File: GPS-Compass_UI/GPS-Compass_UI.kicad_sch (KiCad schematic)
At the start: 12 parts, among them SW1 EXT, SW2 EXT, SW4 EXT

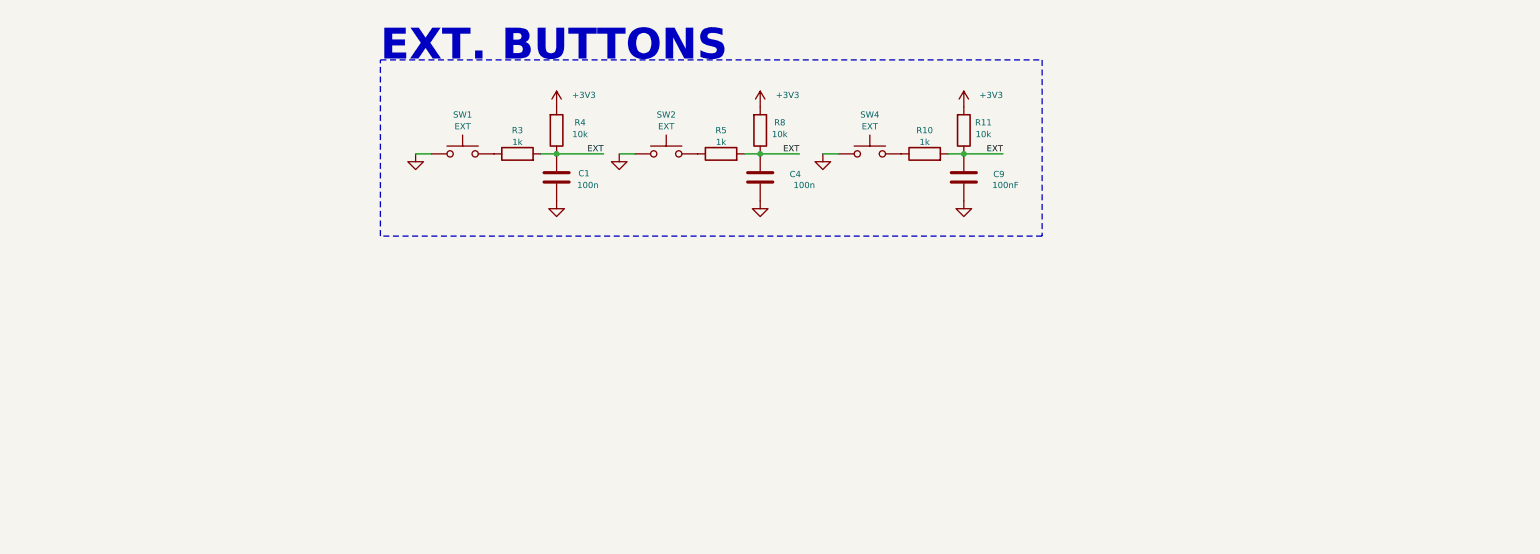
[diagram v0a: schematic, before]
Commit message: UI layout and routing
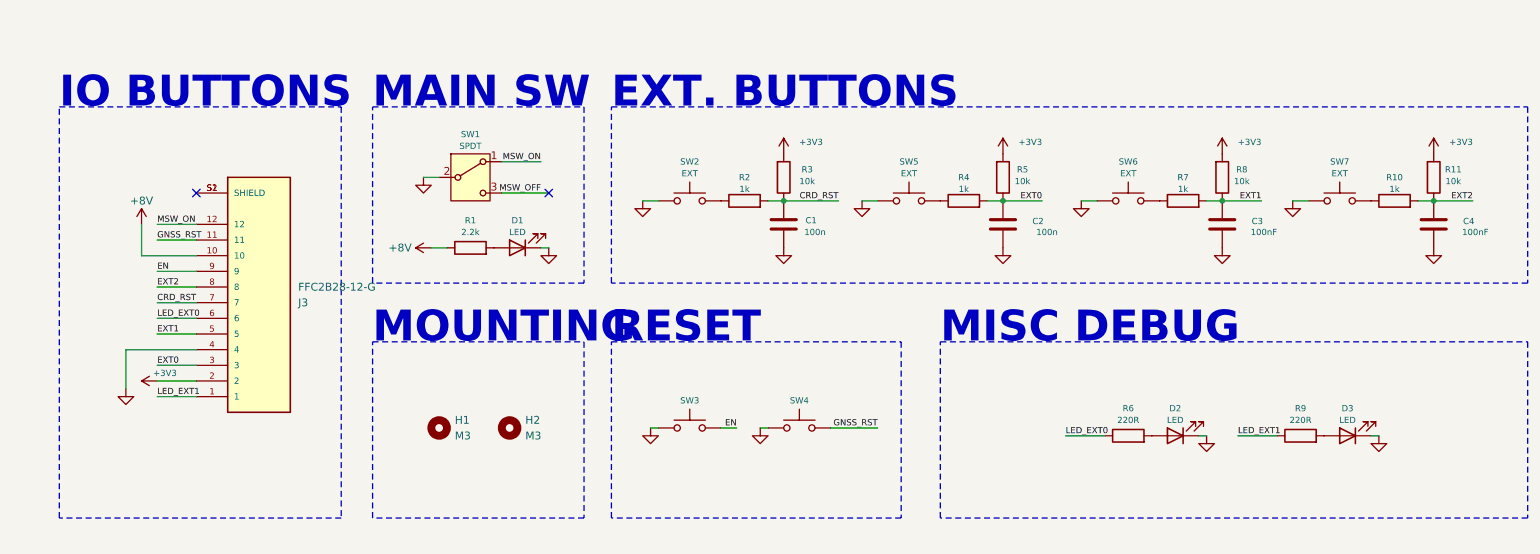
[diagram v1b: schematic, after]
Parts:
- added C4: 100nF, Capacitor_SMD:C_0805_2012Metric, symbol Device:C
- added D1, D2, D3: LED, Connector_Wire:SolderWire-0.1sqmm_1x02_P3.6mm_D0.4mm_OD1mm_Relief, symbol Device:LED
- added H1, H2: M3, MountingHole:MountingHole_3.2mm_M3, symbol Mechanical:MountingHole
- added J3: FFC2B28-12-G, gps-compass_brd:GCT_FFC2B28-12-G, symbol gps-compass_sch:FFC2B28-12-G
- added R1: 2.2k, Resistor_SMD:R_0805_2012Metric, symbol Device:R
- added R10: 1k, Resistor_SMD:R_0805_2012Metric, symbol Device:R
- added R11: 10k, Resistor_SMD:R_0805_2012Metric, symbol Device:R
- added R6, R9: 220R, Resistor_SMD:R_0805_2012Metric, symbol Device:R
- added SW1: SPDT, Connector_Wire:SolderWire-0.1sqmm_1x02_P3.6mm_D0.4mm_OD1mm_Relief, symbol Switch:SW_SPDT
- added SW3, SW4: RESET, Connector_Wire:SolderWire-0.1sqmm_1x02_P3.6mm_D0.4mm_OD1mm_Relief, symbol Switch:SW_Push
- added SW7: EXT, Connector_Wire:SolderWire-0.1sqmm_1x02_P3.6mm_D0.4mm_OD1mm_Relief, symbol Switch:SW_Push
- renumbered C4 to C2, C9 to C3, R3 to R2, R4 to R3, R5 to R4, R8 to R5, R10 to R7, R11 to R8, SW1 to SW2, SW2 to SW5, SW4 to SW6
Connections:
- net +3V3: now also J3.2, R11.2
- net GND: now also C4.1, D1.1 (K), D2.1 (K), D3.1 (K), J3.4, SW1.2 (B), SW3.1, SW4.1, SW7.1
- removed net EXT: C1.2, C2.2, C3.2, R2.2, R3.1, R4.2, R5.1, R7.2, R8.1
- new net: D1.2 (A), R1.2
- new net: D3.2 (A), R9.2
- new net: R10.1, SW7.2
- new net: J3.S1 (SHIELD), J3.S2 (SHIELD)
- new net: D2.2 (A), R6.2
- new net +8V: J3.10, R1.1
- new net CRD_RST: C1.2, J3.7, R2.2, R3.1
- new net EN: J3.9, SW3.2
- new net EXT0: C2.2, J3.3, R4.2, R5.1
- new net EXT1: C3.2, J3.5, R7.2, R8.1
- new net EXT2: C4.2, J3.8, R10.2, R11.1
- new net GNSS_RST: J3.11, SW4.2
- new net LED_EXT0: J3.6, R6.1
- new net LED_EXT1: J3.1, R9.1
- new net MSW_OFF: SW1.3 (C)
- new net MSW_ON: J3.12, SW1.1 (A)
- no-connect marks 0 -> 2
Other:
- note added: "IO BUTTONS"
- note added: "MAIN SW"
- note added: "MISC DEBUG"
- note added: "MOUNTING"
- note added: "RESET"
- moved on the sheet: C1, C2, C3, R2, R3, R4, R5, R7, R8, SW2, SW5, SW6

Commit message: GPS Compass - schematic
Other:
- note added: "FFC"
- note removed: "IO BUTTONS"
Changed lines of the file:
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@@
 		)
 	)
-	(text "IO BUTTONS"
+	(text "FFC"
 		(exclude_from_sim no)
 		(at 31.115 52.705 0)
@@
 		(dnp no)
 		(property "Reference" "J3"
-			(at 69.85 83.8201 0)
+			(at 54.61 106.045 0)
 			(effects
 				(font
@@
 		)
 		(property "Value" "FFC2B28-12-G"
-			(at 69.85 81.2801 0)
-			(effects
-				(font
+			(at 54.61 103.505 0)
+			(effects
+				(font

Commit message: UI changes
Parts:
- removed D3: LED, Connector_Wire:SolderWire-0.1sqmm_1x02_P3.6mm_D0.4mm_OD1mm_Relief, symbol Device:LED
- removed R9: 220R, Resistor_SMD:R_0805_2012Metric, symbol Device:R
- added D1: LED, Connector_Wire:SolderWire-0.1sqmm_1x02_P3.6mm_D0.4mm_OD1mm_Relief, symbol Device:LED
- added R2: 2.2k, Resistor_SMD:R_0805_2012Metric, symbol Device:R
- added SW2: SW_SPDT, Connector_Wire:SolderWire-0.1sqmm_1x02_P3.6mm_D0.4mm_OD1mm_Relief, symbol Switch:SW_SPDT
- renumbered D1 to D2, D2 to D3, J3 to J1, R2 to R3, R3 to R4, R4 to R5, R5 to R6, R6 to R7, R7 to R8, R8 to R9, SW2 to SW3, SW3 to SW4, SW4 to SW5, SW5 to SW6, SW6 to SW7, SW7 to SW8
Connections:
- net +3V3: now also R1.1, SW2.2 (B)
- net GND: now also D1.1 (K); no longer D2.1 (K)
- net GNSS_RST: now also J1.10; no longer J1.11
- net MSW_ON: now also D2.1 (K), J1.11; no longer J1.12
- net DB_1: now reaches R3.1, SW3.2
- net DB_3: now reaches R8.1, SW7.2
- net DB_0: now reaches R10.1, SW8.2
- net DB_2: now reaches R5.1, SW6.2
- removed net +8V: J1.10, R1.1
- net CRD_RST renamed DBNCD_1
- net EXT0 renamed DBNCD_2
- net DBNCD_2: now also J1.5; no longer J1.3
- net EXT1 renamed DBNCD_3
- net DBNCD_3: now also J1.3; no longer J1.5
- net EXT2 renamed DBNCD_0
- net LED_EXT0 renamed LED_EXT
- net LED_EXT1 renamed OTG_ON
- net OTG_ON: now also R2.1, SW2.1 (A)
- new net: D1.2 (A), R2.2
- new net OTG_OFF: SW2.3 (C)
- no-connect marks 2 -> 3
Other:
- note added: "LED"
- note removed: "MISC DEBUG"
- moved on the sheet: C1, C2, C3, C4, D2, D3, H1, H2, J1, R1, R10, R11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

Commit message: jkolsd
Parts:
- renumbered C4 to C1, C1 to C2, C2 to C3, C3 to C4, R8 to R10, R9 to R11, R10 to R3, R11 to R4, R3 to R5, R4 to R6, R5 to R8, R6 to R9, SW4 to SW3, SW8 to SW4, SW3 to SW6, SW6 to SW7, SW7 to SW8
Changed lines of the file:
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@@
 		(on_board yes)
 		(dnp no)
-		(property "Reference" "#PWR020"
+		(property "Reference" "#PWR010"
 			(at 143.51 62.23 0)
 			(effects
@@
 			(project "GPS-Compass_UI"
 				(path "/2171b68c-3635-466a-9c8f-785127caa9a5"
-					(reference "#PWR020")
+					(reference "#PWR010")
 					(unit 1)
 				)
@@
 		(on_board yes)
 		(dnp no)
-		(property "Reference" "SW4"
+		(property "Reference" "SW3"
 			(at 125.73 99.695 0)
 			(effects
@@
 			(project "GPS-Compass_UI"
 				(path "/2171b68c-3635-466a-9c8f-785127caa9a5"
-					(reference "SW4")
+					(reference "SW3")
 					(unit 1)
 				)
@@
 		(on_board yes)
 		(dnp no)
-		(property "Reference" "SW3"
+		(property "Reference" "SW6"
 			(at 162.56 59.69 0)
 			(effects
@@
 			(project "GPS-Compass_UI"
 				(path "/2171b68c-3635-466a-9c8f-785127caa9a5"
-					(reference "SW3")
+					(reference "SW6")
 					(unit 1)
 				)
@@
 		(on_board yes)
 		(dnp no)
-		(property "Reference" "R11"
+		(property "Reference" "R4"
 			(at 146.685 60.96 0)
 			(effects
@@
 			(project "GPS-Compass_UI"
 				(path "/2171b68c-3635-466a-9c8f-785127caa9a5"
-					(reference "R11")
+					(reference "R4")
 					(unit 1)
 				)
@@
 		(on_board yes)
 		(dnp no)
-		(property "Reference" "SW7"
+		(property "Reference" "SW8"
 			(at 228.6 59.69 0)
 			(effects
@@
 			(project "GPS-Compass_UI"
 				(path "/2171b68c-3635-466a-9c8f-785127caa9a5"
-					(reference "SW7")
+					(reference "SW8")
 					(unit 1)
 				)
@@
 		(on_board yes)
 		(dnp no)
-		(property "Reference" "#PWR010"
+		(property "Reference" "#PWR013"
 			(at 179.07 62.23 0)
 			(effects
@@
 			(project "GPS-Compass_UI"
 				(path "/2171b68c-3635-466a-9c8f-785127caa9a5"
-					(reference "#PWR010")
+					(reference "#PWR013")
 					(unit 1)
 				)
@@
 		(on_board yes)
 		(dnp no)
-		(property "Reference" "C3"
+		(property "Reference" "C4"
 			(at 250.19 69.215 0)
 			(effects
@@
 			(project "GPS-Compass_UI"
 				(path "/2171b68c-3635-466a-9c8f-785127caa9a5"
-					(reference "C3")
+					(reference "C4")
 					(unit 1)
 				)
@@
 		(on_board yes)
 		(dnp no)
-		(property "Reference" "R8"
+		(property "Reference" "R10"
 			(at 238.76 62.23 90)
 			(effects
@@
 			(project "GPS-Compass_UI"
 				(path "/2171b68c-3635-466a-9c8f-785127caa9a5"
-					(reference "R8")
+					(reference "R10")
 					(unit 1)
 				)
@@
 		(on_board yes)
 		(dnp no)
-		(property "Reference" "C2"
+		(property "Reference" "C3"
 			(at 216.535 69.215 0)
 			(effects
@@
 			(project "GPS-Compass_UI"
 				(path "/2171b68c-3635-466a-9c8f-785127caa9a5"
-					(reference "C2")
+					(reference "C3")
 					(unit 1)
 				)
@@
 		(on_board yes)
 		(dnp no)
-		(property "Reference" "C4"
+		(property "Reference" "C1"
 			(at 148.59 69.215 0)
 			(effects
@@
 			(project "GPS-Compass_UI"
 				(path "/2171b68c-3635-466a-9c8f-785127caa9a5"
-					(reference "C4")
+					(reference "C1")
 					(unit 1)
 				)
@@
 		(on_board yes)
 		(dnp no)
-		(property "Reference" "#PWR017"
+		(property "Reference" "#PWR020"
 			(at 245.11 62.23 0)
 			(effects
@@
 			(project "GPS-Compass_UI"
 				(path "/2171b68c-3635-466a-9c8f-785127caa9a5"
-					(reference "#PWR017")
+					(reference "#PWR020")
 					(unit 1)
 				)
@@
 		(on_board yes)
 		(dnp no)
-		(property "Reference" "#PWR011"
+		(property "Reference" "#PWR014"
 			(at 179.07 80.01 0)
 			(effects
@@
 			(project "GPS-Compass_UI"
 				(path "/2171b68c-3635-466a-9c8f-785127caa9a5"
-					(reference "#PWR011")
+					(reference "#PWR014")
 					(unit 1)
 				)
@@
 		(on_board yes)
 		(dnp no)
-		(property "Reference" "SW8"
+		(property "Reference" "SW4"
 			(at 127 59.69 0)
 			(effects
@@
 			(project "GPS-Compass_UI"
 				(path "/2171b68c-3635-466a-9c8f-785127caa9a5"
-					(reference "SW8")
+					(reference "SW4")
 					(unit 1)
 				)
@@
 		(on_board yes)
 		(dnp no)
-		(property "Reference" "R9"
+		(property "Reference" "R11"
 			(at 248.285 60.96 0)
 			(effects
@@
 			(project "GPS-Compass_UI"
 				(path "/2171b68c-3635-466a-9c8f-785127caa9a5"
-					(reference "R9")
+					(reference "R11")
 					(unit 1)
 				)
@@
 		(on_board yes)
 		(dnp no)
-		(property "Reference" "SW6"
+		(property "Reference" "SW7"
 			(at 195.58 59.69 0)
 			(effects
@@
 			(project "GPS-Compass_UI"
 				(path "/2171b68c-3635-466a-9c8f-785127caa9a5"
-					(reference "SW6")
+					(reference "SW7")
 					(unit 1)
 				)
@@
 		(on_board yes)
 		(dnp no)
-		(property "Reference" "#PWR015"
+		(property "Reference" "#PWR019"
 			(at 222.25 72.39 0)
 			(effects
@@
 			(project "GPS-Compass_UI"
 				(path "/2171b68c-3635-466a-9c8f-785127caa9a5"
-					(reference "#PWR015")
+					(reference "#PWR019")
 					(unit 1)
 				)
@@
 		(on_board yes)
 		(dnp no)
-		(property "Reference" "#PWR014"
+		(property "Reference" "#PWR018"
 			(at 212.09 80.01 0)
 			(effects
@@
 			(project "GPS-Compass_UI"
 				(path "/2171b68c-3635-466a-9c8f-785127caa9a5"
-					(reference "#PWR014")
+					(reference "#PWR018")
 					(unit 1)
 				)
@@
 		(on_board yes)
 		(dnp no)
-		(property "Reference" "R6"
+		(property "Reference" "R9"
 			(at 215.265 60.96 0)
 			(effects
@@
 			(project "GPS-Compass_UI"
 				(path "/2171b68c-3635-466a-9c8f-785127caa9a5"
-					(reference "R6")
+					(reference "R9")
 					(unit 1)
 				)
@@
 		(on_board yes)
 		(dnp no)
-		(property "Reference" "C1"
+		(property "Reference" "C2"
 			(at 182.88 69.215 0)
 			(effects
@@
 			(project "GPS-Compass_UI"
 				(path "/2171b68c-3635-466a-9c8f-785127caa9a5"
-					(reference "C1")
+					(reference "C2")
 					(unit 1)
 				)
@@
 		(on_board yes)
 		(dnp no)
-		(property "Reference" "R5"
+		(property "Reference" "R8"
 			(at 205.74 62.23 90)
 			(effects
@@
 			(project "GPS-Compass_UI"
 				(path "/2171b68c-3635-466a-9c8f-785127caa9a5"
-					(reference "R5")
+					(reference "R8")
 					(unit 1)
 				)
@@
 		(on_board yes)
 		(dnp no)
-		(property "Reference" "#PWR013"
+		(property "Reference" "#PWR017"
 			(at 212.09 62.23 0)
 			(effects
@@
 			(project "GPS-Compass_UI"
 				(path "/2171b68c-3635-466a-9c8f-785127caa9a5"
-					(reference "#PWR013")
+					(reference "#PWR017")
 					(unit 1)
 				)
@@
 		(on_board yes)
 		(dnp no)
-		(property "Reference" "#PWR08"
+		(property "Reference" "#PWR07"
 			(at 119.38 110.49 0)
 			(effects
@@
 			(project "GPS-Compass_UI"
 				(path "/2171b68c-3635-466a-9c8f-785127caa9a5"
-					(reference "#PWR08")
+					(reference "#PWR07")
 					(unit 1)
 				)
@@
 		(on_board yes)
 		(dnp no)
-		(property "Reference" "#PWR07"
+		(property "Reference" "#PWR012"
 			(at 156.21 72.39 0)
 			(effects
@@
 			(project "GPS-Compass_UI"
 				(path "/2171b68c-3635-466a-9c8f-785127caa9a5"
-					(reference "#PWR07")
+					(reference "#PWR012")
 					(unit 1)
 				)
@@
 		(on_board yes)
 		(dnp no)
-		(property "Reference" "#PWR012"
+		(property "Reference" "#PWR015"
 			(at 189.23 72.39 0)
 			(effects
@@
 			(project "GPS-Compass_UI"
 				(path "/2171b68c-3635-466a-9c8f-785127caa9a5"
-					(reference "#PWR012")
+					(reference "#PWR015")
 					(unit 1)
 				)
@@
 		(on_board yes)
 		(dnp no)
-		(property "Reference" "R4"
+		(property "Reference" "R6"
 			(at 182.88 60.96 0)
 			(effects
@@
 			(project "GPS-Compass_UI"
 				(path "/2171b68c-3635-466a-9c8f-785127caa9a5"
-					(reference "R4")
+					(reference "R6")
 					(unit 1)
 				)
@@
 		(on_board yes)
 		(dnp no)
-		(property "Reference" "#PWR018"
+		(property "Reference" "#PWR021"
 			(at 245.11 80.01 0)
 			(effects
@@
 			(project "GPS-Compass_UI"
 				(path "/2171b68c-3635-466a-9c8f-785127caa9a5"
-					(reference "#PWR018")
+					(reference "#PWR021")
 					(unit 1)
 				)
@@
 		(on_board yes)
 		(dnp no)
-		(property "Reference" "#PWR021"
+		(property "Reference" "#PWR011"
 			(at 143.51 80.01 0)
 			(effects
@@
 			(project "GPS-Compass_UI"
 				(path "/2171b68c-3635-466a-9c8f-785127caa9a5"
-					(reference "#PWR021")
+					(reference "#PWR011")
 					(unit 1)
 				)
@@
 		(on_board yes)
 		(dnp no)
-		(property "Reference" "R10"
+		(property "Reference" "R3"
 			(at 137.16 62.23 90)
 			(effects
@@
 			(project "GPS-Compass_UI"
 				(path "/2171b68c-3635-466a-9c8f-785127caa9a5"
-					(reference "R10")
+					(reference "R3")
 					(unit 1)
 				)
@@
 		(on_board yes)
 		(dnp no)
-		(property "Reference" "R3"
+		(property "Reference" "R5"
 			(at 172.72 62.23 90)
 			(effects
@@
 			(project "GPS-Compass_UI"
 				(path "/2171b68c-3635-466a-9c8f-785127caa9a5"
-					(reference "R3")
+					(reference "R5")
 					(unit 1)
 				)
@@
 		(on_board yes)
 		(dnp no)
-		(property "Reference" "#PWR019"
+		(property "Reference" "#PWR08"
 			(at 120.65 72.39 0)
 			(effects
@@
 			(project "GPS-Compass_UI"
 				(path "/2171b68c-3635-466a-9c8f-785127caa9a5"
-					(reference "#PWR019")
+					(reference "#PWR08")
 					(unit 1)
 				)

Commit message: asdasd
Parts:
- SW2: footprint Connector_Wire:SolderWire-0.1sqmm_1x02_P3.6mm_D0.4mm_OD1mm_Relief -> Connector_Wire:SolderWire-0.1sqmm_1x03_P3.6mm_D0.4mm_OD1mm_Relief
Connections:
- net DBNCD_0: now also J1.9; no longer J1.8
- net DBNCD_1: now also J1.8; no longer J1.7
- net DBNCD_2: now also J1.6; no longer J1.5
- net DBNCD_3: now also J1.5; no longer J1.3
- net EN: now also J1.10; no longer J1.9
- net GND: now also J1.1; no longer J1.4
- net GNSS_RST: now also J1.11; no longer J1.10
- net LED_EXT: now also J1.7; no longer J1.6
- net MSW_ON: now also J1.12; no longer J1.11
- net OTG_OFF renamed SINK-MODE
- net SINK-MODE: now also J1.3
- net OTG_ON renamed SRC-MODE
- net SRC-MODE: now also J1.4; no longer J1.1
- no-connect marks 3 -> 2
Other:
- note added: "OTG SW"

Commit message: i think im depressed again
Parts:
- removed SW2: SW_SPDT, Connector_Wire:SolderWire-0.1sqmm_1x03_P3.6mm_D0.4mm_OD1mm_Relief, symbol Switch:SW_SPDT
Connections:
- net SINK-MODE is gone; now on net GND: J1.3
- net SRC-MODE renamed OTG
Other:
- note removed: "OTG SW"
- moved on the sheet: D3, R7

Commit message: asdasd
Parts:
- removed D1: LED, Connector_Wire:SolderWire-0.1sqmm_1x02_P3.6mm_D0.4mm_OD1mm_Relief, symbol Device:LED
- removed J1: FFC2B28-12-G, gps-compass_brd:GCT_FFC2B28-12-G, symbol gps-compass_sch:FFC2B28-12-G
- removed R2: 2.2k, Resistor_SMD:R_0805_2012Metric, symbol Device:R
- added J4: Conn_01x10_Socket, Connector_PinHeader_2.54mm:PinHeader_1x10_P2.54mm_Horizontal, symbol Connector:Conn_01x10_Socket
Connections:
- net +3V3: now also J4.10 (Pin_10)
- net DBNCD_0: now also J4.2 (Pin_2)
- net DBNCD_1: now also J4.3 (Pin_3)
- net DBNCD_2: now also J4.5 (Pin_5)
- net DBNCD_3: now also J4.6 (Pin_6)
- net EN: now also SW3.1, J4.8 (Pin_8); no longer SW3.2
- net GND: now also SW3.2, SW5.2, J4.9 (Pin_9); no longer SW3.1, SW5.1
- net GNSS_RST: now also SW5.1, J4.1 (Pin_1); no longer SW5.2
- net LED_EXT: now also J4.4 (Pin_4)
- net MSW_ON: now also J4.7 (Pin_7)
- no-connect marks 2 -> 1
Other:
- note added: "CONN"
- note removed: "FFC"
- moved on the sheet: D3, R7

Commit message: UI board updates
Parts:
- removed H1, H2: M3, MountingHole:MountingHole_3.2mm_M3, symbol Mechanical:MountingHole
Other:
- note removed: "MOUNTING"
- moved on the sheet: C1, C2, C3, C4, D2, D3, J4, R1, R10, R11, R3, R4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
